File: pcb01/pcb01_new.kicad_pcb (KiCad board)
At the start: 2 copper layers, 119.4 x 91.4 mm, 60 parts, among them J1 DIN41612_02x32_AC, J10 PLD_aux, J11 Conn_01x09, J2 Jmp_UART_Irq, J3 Conn_01x09_Socket, J4 Conn_01x08_Socket, J5 UART, J6 Conn_01x02_Socket, J7 Jmp_Irq, J8 Jmp_NMI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

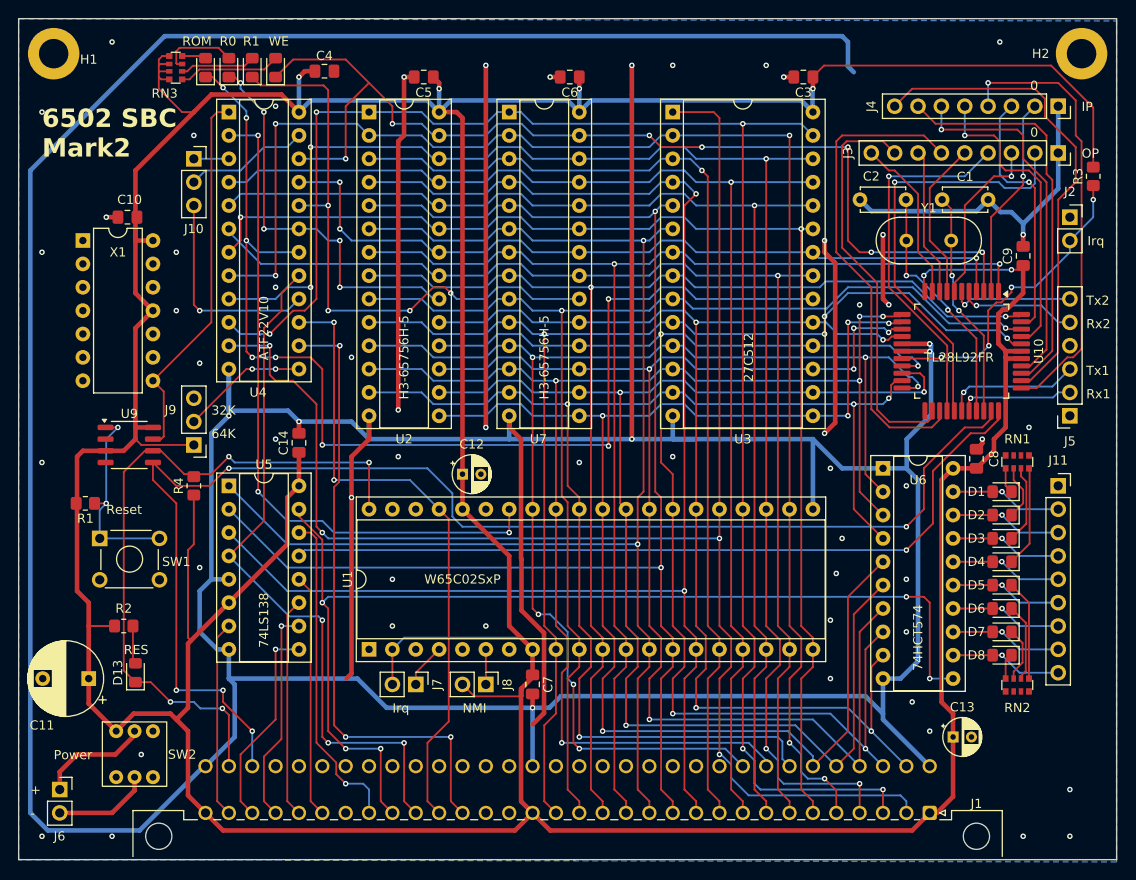
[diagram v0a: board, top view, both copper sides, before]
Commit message: tested addrdec v3 & ordered mark2 board :-O
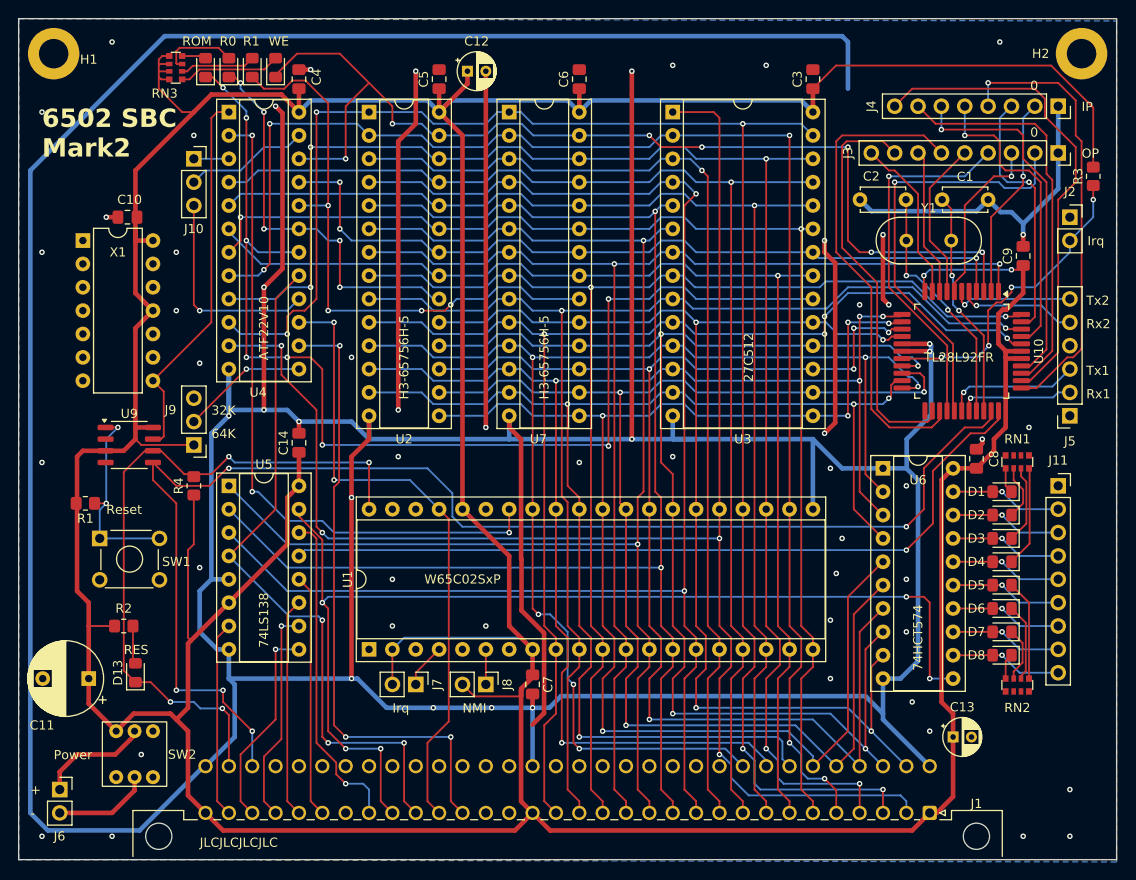
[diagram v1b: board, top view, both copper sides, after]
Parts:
- moved C12 43.8 mm to (71.7, 21.0)
- moved C4 2.91 mm to (53.3, 21.8), turned to 90 degrees
- moved C5 1.69 mm to (68.6, 21.8), turned to 90 degrees
- moved C3 1.06 mm to (109.2, 21.8), turned to 90 degrees
- moved C6 1.06 mm to (83.8, 21.8), turned to 90 degrees
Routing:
- net GND: track 733.8 -> 767.1 mm, vias 61 -> 62
- net VCC: track 581.2 -> 579.0 mm, vias 6 -> 2
- net /~{CS_RAM1}: track 65.9 -> 64.8 mm
- net /A14: track 178.1 -> 179.3 mm
- net /~{QWE_RAM}: track 113.2 -> 113.9 mm
- net /A12: track 158.0 -> 157.2 mm
- net Net-(J9-Pin_2): vias 2 -> 1
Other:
- board text added: "JLCJLCJLCJLC"

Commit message: connect rw to external connector
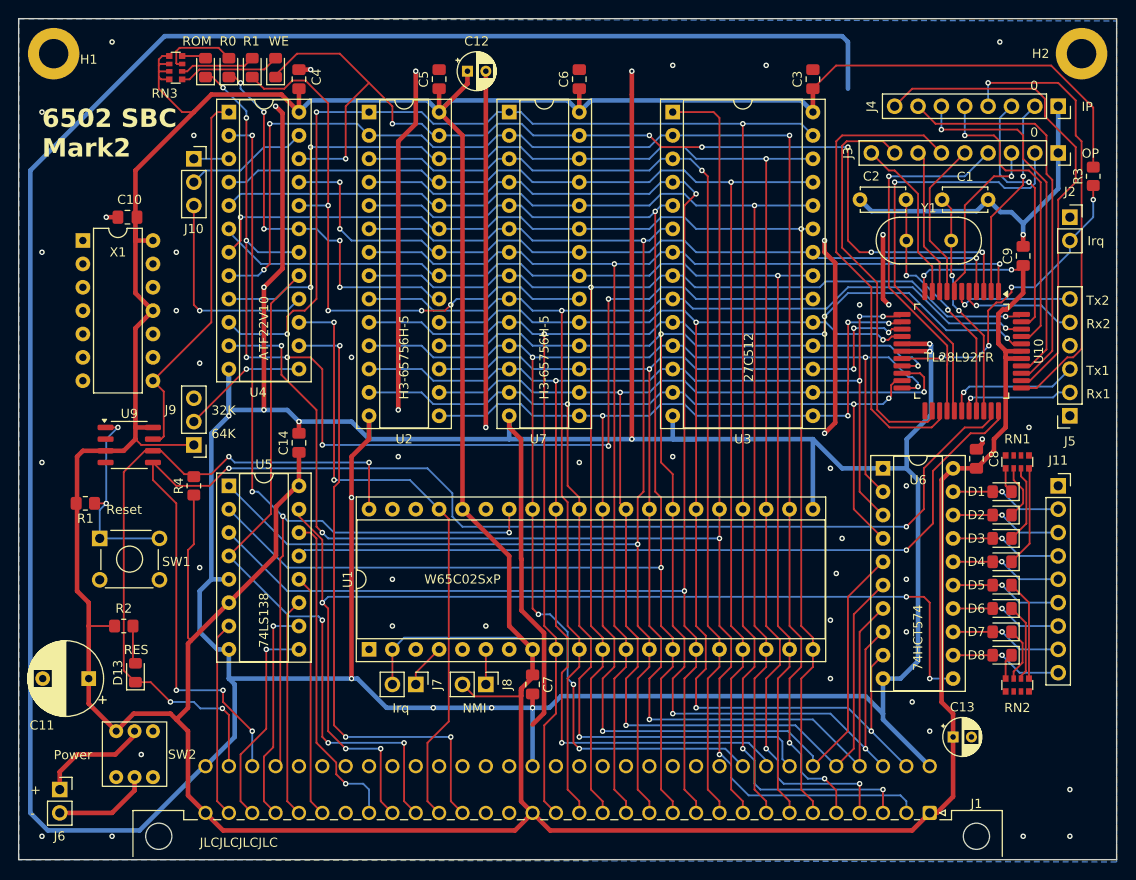
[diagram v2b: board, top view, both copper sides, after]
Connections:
- J1 pad c29: unconnected-(J1-Pin_c29-Padc29) -> /R/~{W}
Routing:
- net /R/~{W}: track 73.6 -> 101.1 mm, vias 3 -> 4
- net /~{IOEN_06}: track 22.4 -> 23.0 mm
- net /~{IOEN_05}: track 23.5 -> 24.1 mm
